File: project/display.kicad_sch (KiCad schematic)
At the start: 0 parts

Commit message: schemtic is done, need to go through BOM
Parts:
- added J6: 16 PIN SOLDER PIN, symbol bozi:SOLDER_PAD_16_PINS
- added R48, R49, R50, R51, R52, R53, R54, R55, R56, R57, R58, R59, R60, R61: 30R, bozi:RESC1005X37N_edit, symbol Device:R
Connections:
- new net: J6.5, R58.1
- new net: J6.15, R48.1
- new net: J6.4, R59.1
- new net: J6.3, R60.1
- new net: J6.12, R51.1
- new net: J6.10, R53.1
- new net: J6.11, R52.1
- new net: J6.13, R50.1
- new net: J6.14, R49.1
- new net: J6.2, R61.1
- new net: J6.6, R57.1
- new net: J6.7, R56.1
- new net: J6.8, R55.1
- new net: J6.9, R54.1
- new net GNDREF: J6.1, J6.16
- new net LCD_CSX: R59.2
- new net LCD_DAT0: R55.2
- new net LCD_DAT1: R54.2
- new net LCD_DAT2: R53.2
- new net LCD_DAT3: R52.2
- new net LCD_DAT4: R51.2
- new net LCD_DAT5: R50.2
- new net LCD_DAT6: R49.2
- new net LCD_DAT7: R48.2
- new net LCD_D/CX: R58.2
- new net LCD_RDX: R56.2
- new net LCD_RESX: R61.2
- new net LCD_TE: R60.2
- new net LCD_WRX: R57.2
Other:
- note added: "All resistor are 30 Ohms"
- note added: "Backlight voltage regulator"

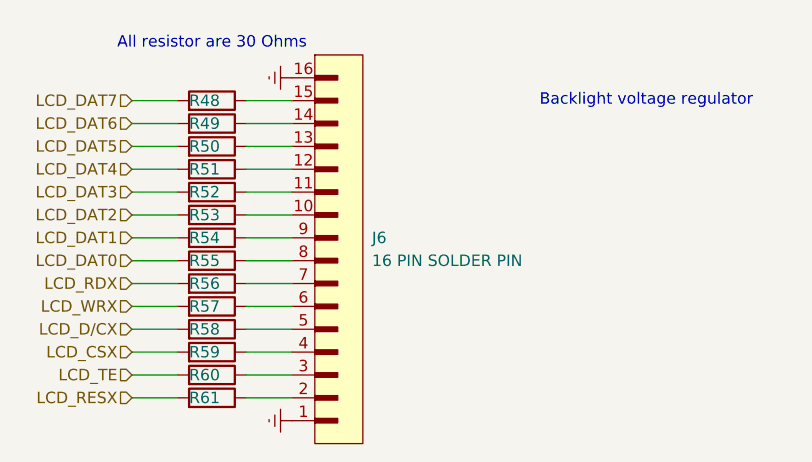
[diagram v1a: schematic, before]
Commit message: schemtic is done, annotation set
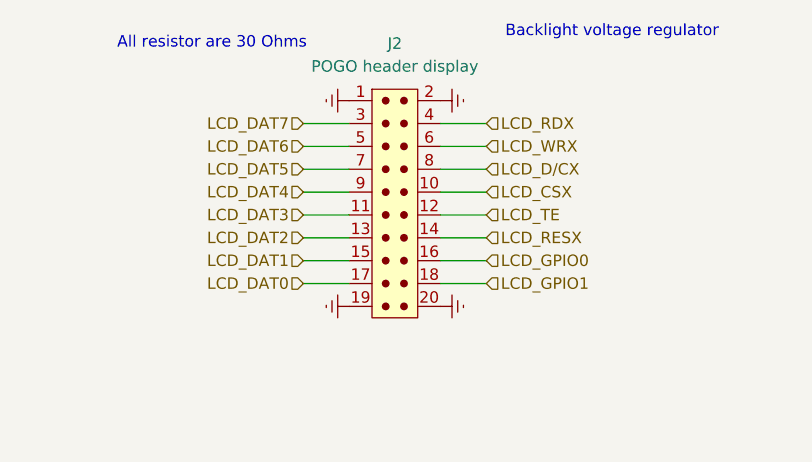
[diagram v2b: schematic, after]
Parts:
- removed J6: 16 PIN SOLDER PIN, symbol bozi:SOLDER_PAD_16_PINS
- removed R48, R49, R50, R51, R52, R53, R54, R55, R56, R57, R58, R59, R60, R61: 30R, bozi:RESC1005X37N_edit, symbol Device:R
- added J2: POGO header display, bozi:8552202030001101_edit, symbol bozi:POGO_20P
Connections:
- net GNDREF: now also J2.1, J2.19, J2.2, J2.20
- net LCD_CSX: now also J2.10
- net LCD_DAT0: now also J2.17
- net LCD_DAT1: now also J2.15
- net LCD_DAT2: now also J2.13
- net LCD_DAT3: now also J2.11
- net LCD_DAT4: now also J2.9
- net LCD_DAT5: now also J2.7
- net LCD_DAT6: now also J2.5
- net LCD_DAT7: now also J2.3
- net LCD_D/CX: now also J2.8
- net LCD_RDX: now also J2.4
- net LCD_RESX: now also J2.14
- net LCD_TE: now also J2.12
- net LCD_WRX: now also J2.6
- new net LCD_GPIO0: J2.16
- new net LCD_GPIO1: J2.18
